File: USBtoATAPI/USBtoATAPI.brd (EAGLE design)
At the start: 68 x 20 mm, 3 parts, among them J2 10118192-0002LF

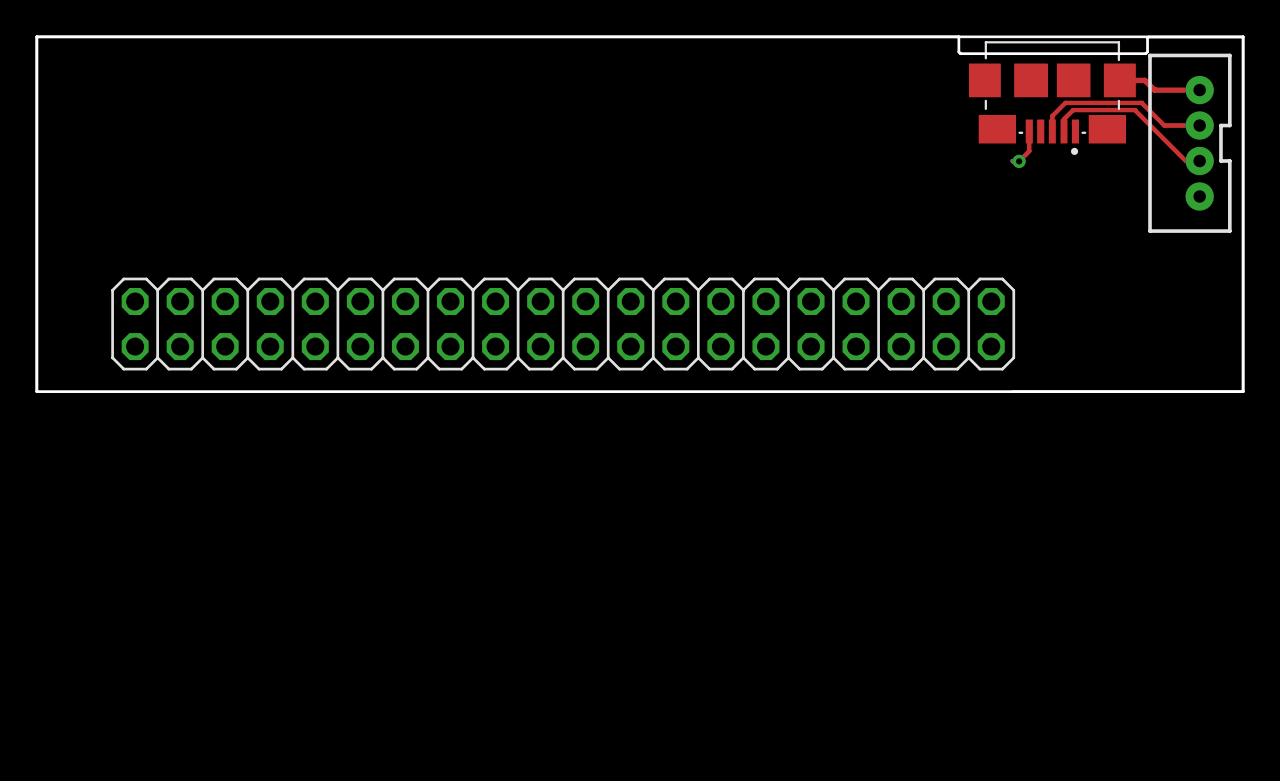
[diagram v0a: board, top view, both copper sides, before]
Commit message: Started layout
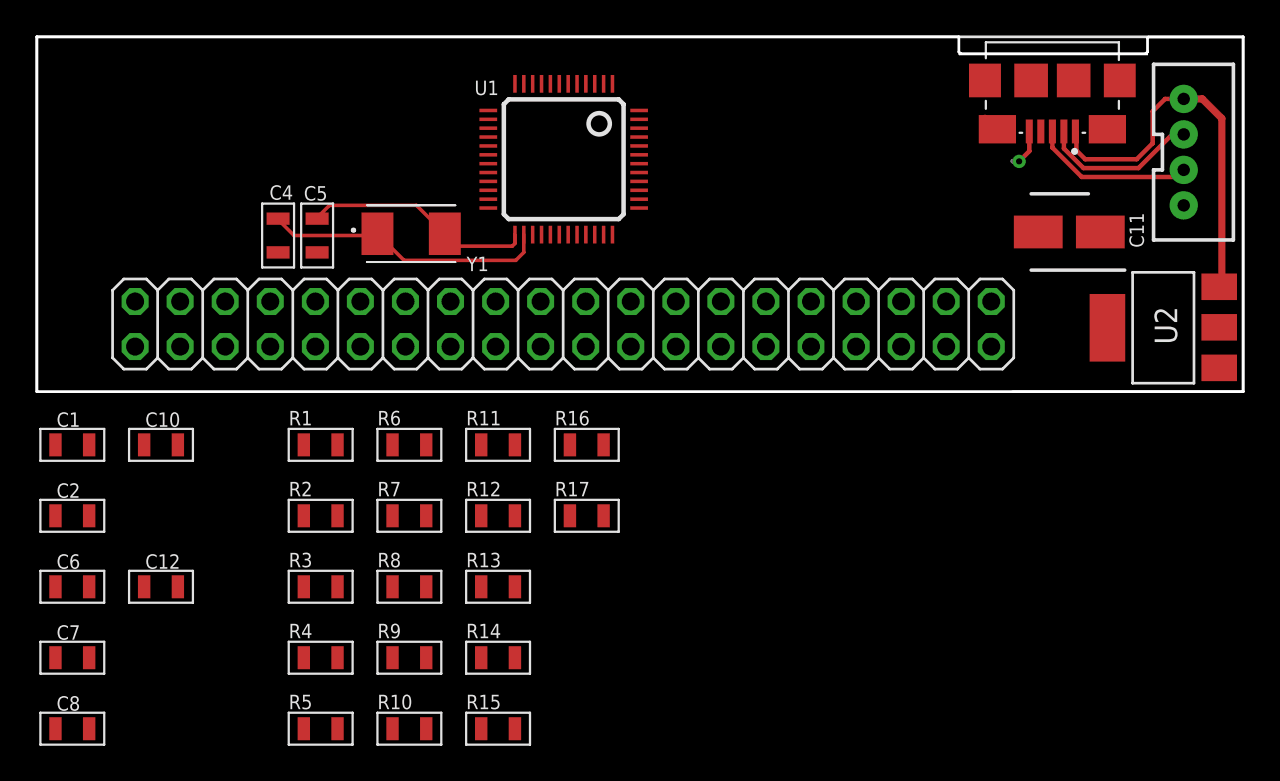
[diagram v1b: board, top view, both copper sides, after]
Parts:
- added C1: 120pF, MF_Passives:C0805
- added C10: 1nF, MF_Passives:C0805
- added C11: 47uF, SamacSys_Parts:CAPAE430X550N
- added C12: 220pF, MF_Passives:C0805
- added C2, C4, C5: 22pF, MF_Passives:C0805
- added C6, C7, C8: 100nF, MF_Passives:C0805
- added R1, R2: 100k, MF_Passives:R0805
- added R10, R12: 33, MF_Passives:R0805
- added R11, R13: 10, MF_Passives:R0805
- added R14: 510k, MF_Passives:R0805
- added R15: 33k, MF_Passives:R0805
- added R16: 20k, MF_Passives:R0805
- added R17, R7: 330k, MF_Passives:R0805
- added R3, R4, R5, R6: 10k, MF_Passives:R0805
- added R8: 1.5k, MF_Passives:R0805
- added R9: 510, MF_Passives:R0805
- added U1: GL811E, GenesisLogic:LQFP-48
- added U2: REG1117, burr-brown:SOT223
- added Y1: 445C33C12M00000, SamacSys_Parts:445C33C12M00000
- moved J1 0.54 mm to (65.2, 13.5), turned to 270 degrees
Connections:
- new net N$1: C4.P$1, U1.26, Y1.1
- new net N$2: C5.P$2, U1.25, Y1.2
- new net VCC: U2.2
- net DATA0: now also U1.38, U1.39
- net DATA1: now also U1.40
- net DATA10: now also U1.4
- net DATA11: now also U1.5
- net DATA12: now also U1.8
- net DATA13: now also U1.9
- net DATA14: now also U1.10
- net DATA15: now also U1.11
- net DATA3: now also U1.41
- net DATA4: now also U1.44
- net DATA5: now also U1.45
- net DATA6: now also U1.46
- net DATA7: now also U1.47
- net DATA8: now also U1.2
- net DATA9: now also U1.3
- net GND: now also C4.P$2, C5.P$1, U2.1
- net VUSB: now also U2.3
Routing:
- net VUSB: track 0.00 -> 22.0 mm
- net N$1: track 0.00 -> 16.1 mm
- net N$2: track 0.00 -> 13.2 mm
- net GND: track 8.02 -> 3.29 mm
- net D+: track 10.0 -> 9.17 mm
- net D-: track 9.74 -> 8.96 mm
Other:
- outline, holes or cut-outs redrawn
